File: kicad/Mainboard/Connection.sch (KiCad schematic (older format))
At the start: 12 parts, among them J13 DBG_CONN, J15 Micro_SD_Card

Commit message: Annotated parts, again.
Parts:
- gave numbers to parts that had none: 10
- renumbered J15 to J14, J13 to J15
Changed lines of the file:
@@
 EESchema Schematic File Version 4
-LIBS:Mainboard-cache
 EELAYER 30 0
 EELAYER END
@@
 $EndDescr
 $Comp
-L power:+5V #PWR0104
+L power:+5V #PWR0155
 U 1 1 5E07BDC5
 P 3000 1750
-F 0 "#PWR0104" H 3000 1600 50  0001 C CNN
+F 0 "#PWR0155" H 3000 1600 50  0001 C CNN
 F 1 "+5V" H 3015 1923 50  0000 C CNN
 F 2 "" H 3000 1750 50  0001 C CNN
@@
 	3000 1850 3100 1850
 $Comp
-L power:GND #PWR0106
+L power:GND #PWR0156
 U 1 1 5E07C3FA
 P 3000 2350
-F 0 "#PWR0106" H 3000 2100 50  0001 C CNN
+F 0 "#PWR0156" H 3000 2100 50  0001 C CNN
 F 1 "GND" H 3005 2177 50  0000 C CNN
 F 2 "" H 3000 2350 50  0001 C CNN
@@
 USART1_RX
 $Comp
-L Mainboard-rescue:Conn_01x03-conn J13
+L Mainboard-rescue:Conn_01x03-conn J15
 U 1 1 5E07CB74
 P 4800 2150
-F 0 "J13" H 4880 2192 50  0000 L CNN
+F 0 "J15" H 4880 2192 50  0000 L CNN
 F 1 "DBG_CONN" H 4880 2101 50  0000 L CNN
 F 2 "" H 4800 2150 50  0001 C CNN
@@
 USART2_RX
 $Comp
-L power:GND #PWR0107
+L power:GND #PWR0157
 U 1 1 5E07D3F6
 P 4500 2350
-F 0 "#PWR0107" H 4500 2100 50  0001 C CNN
+F 0 "#PWR0157" H 4500 2100 50  0001 C CNN
 F 1 "GND" H 4505 2177 50  0000 C CNN
 F 2 "" H 4500 2350 50  0001 C CNN
@@
 	4500 2050 4600 2050
 $Comp
-L Mainboard-rescue:Micro_SD_Card-conn J15
+L Mainboard-rescue:Micro_SD_Card-conn J14
 U 1 1 5E0856B5
 P 3950 3900
-F 0 "J15" H 3900 4617 50  0000 C CNN
+F 0 "J14" H 3900 4617 50  0000 C CNN
 F 1 "Micro_SD_Card" H 3900 4526 50  0000 C CNN
 F 2 "" H 5100 4200 50  0001 C CNN
@@
 	3050 4100 2950 4100
 $Comp
-L power:GND #PWR0114
+L power:GND #PWR0154
 U 1 1 5E08619F
 P 2950 4600
-F 0 "#PWR0114" H 2950 4350 50  0001 C CNN
+F 0 "#PWR0154" H 2950 4350 50  0001 C CNN
 F 1 "GND" H 2955 4427 50  0000 C CNN
 F 2 "" H 2950 4600 50  0001 C CNN
@@
 	2950 4100 2950 4600
 $Comp
-L power:GND #PWR0115
+L power:GND #PWR0158
 U 1 1 5E086C12
 P 4850 4600
-F 0 "#PWR0115" H 4850 4350 50  0001 C CNN
+F 0 "#PWR0158" H 4850 4350 50  0001 C CNN
 F 1 "GND" H 4855 4427 50  0000 C CNN
 F 2 "" H 4850 4600 50  0001 C CNN
@@
 	4850 4500 4850 4600
 $Comp
-L power:+3V3 #PWR0109
+L power:+3V3 #PWR0153
 U 1 1 5E087582
 P 2950 3500
-F 0 "#PWR0109" H 2950 3350 50  0001 C CNN
+F 0 "#PWR0153" H 2950 3350 50  0001 C CNN
 F 1 "+3V3" H 2965 3673 50  0000 C CNN
 F 2 "" H 2950 3500 50  0001 C CNN
@@
 ADDR 0x6B AG, 0x1E M
 $Comp
-L Sensor_Motion:LSM9DS1 U?
+L Sensor_Motion:LSM9DS1 U11
 U 1 1 5E067250
 P 8400 3850
-F 0 "U?" H 8400 3900 50  0000 C CNN
+F 0 "U11" H 8400 3900 50  0000 C CNN
 F 1 "LSM9DS1" H 8400 3800 50  0000 C CNN
 F 2 "Package_LGA:LGA-24L_3x3.5mm_P0.43mm" H 9900 4600 50  0001 C CNN
@@
 $EndComp
 $Comp
-L power:+3V3 #PWR?
+L power:+3V3 #PWR0166
 U 1 1 5E06CB2E
 P 8400 2850
-F 0 "#PWR?" H 8400 2700 50  0001 C CNN
+F 0 "#PWR0166" H 8400 2700 50  0001 C CNN
 F 1 "+3V3" H 8415 3023 50  0000 C CNN
 F 2 "" H 8400 2850 50  0001 C CNN
@@
 Connection ~ 8700 2950
 $Comp
-L power:GND #PWR?
+L power:GND #PWR0165
 U 1 1 5E06F5C7
 P 8300 4850
-F 0 "#PWR?" H 8300 4600 50  0001 C CNN
+F 0 "#PWR0165" H 8300 4600 50  0001 C CNN
 F 1 "GND" H 8305 4677 50  0000 C CNN
 F 2 "" H 8300 4850 50  0001 C CNN
@@
 $EndComp
 $Comp
-L power:GND #PWR?
+L power:GND #PWR0167
 U 1 1 5E06FFF0
 P 8500 4850
-F 0 "#PWR?" H 8500 4600 50  0001 C CNN
+F 0 "#PWR0167" H 8500 4600 50  0001 C CNN
 F 1 "GND" H 8505 4677 50  0000 C CNN
 F 2 "" H 8500 4850 50  0001 C CNN
@@
 $EndComp
 $Comp
-L power:GND #PWR?
+L power:GND #PWR0169
 U 1 1 5E070F61
 P 9200 4850
-F 0 "#PWR?" H 9200 4600 50  0001 C CNN
+F 0 "#PWR0169" H 9200 4600 50  0001 C CNN
 F 1 "GND" H 9205 4677 50  0000 C CNN
 F 2 "" H 9200 4850 50  0001 C CNN
@@
 	9200 4050 9200 4150
 $Comp
-L Device:R_Small R?
+L Device:R_Small R54
 U 1 1 5E07451A
 P 7500 3250
-F 0 "R?" H 7559 3296 50  0000 L CNN
+F 0 "R54" H 7559 3296 50  0000 L CNN
 F 1 "4k7" H 7559 3205 50  0000 L CNN
 F 2 "" H 7500 3250 50  0001 C CNN
@@
 $EndComp
 $Comp
-L Device:R_Small R?
+L Device:R_Small R53
 U 1 1 5E075066
 P 7250 3250
-F 0 "R?" H 7309 3296 50  0000 L CNN
+F 0 "R53" H 7309 3296 50  0000 L CNN
 F 1 "4k7" H 7309 3205 50  0000 L CNN
 F 2 "" H 7250 3250 50  0001 C CNN
@@
 Connection ~ 7500 3550
 $Comp
-L power:+3V3 #PWR?
+L power:+3V3 #PWR0163
 U 1 1 5E0788C1
 P 7500 3050
-F 0 "#PWR?" H 7500 2900 50  0001 C CNN
+F 0 "#PWR0163" H 7500 2900 50  0001 C CNN
 F 1 "+3V3" H 7515 3223 50  0000 C CNN
 F 2 "" H 7500 3050 50  0001 C CNN
@@
 $EndComp
 $Comp
-L power:+3V3 #PWR?
+L power:+3V3 #PWR0162
 U 1 1 5E078F90
 P 7250 3050
-F 0 "#PWR?" H 7250 2900 50  0001 C CNN
+F 0 "#PWR0162" H 7250 2900 50  0001 C CNN
 F 1 "+3V3" H 7265 3223 50  0000 C CNN
 F 2 "" H 7250 3050 50  0001 C CNN
@@
 	7500 3050 7500 3150
 $Comp
-L Device:C_Small C?
+L Device:C_Small C93
 U 1 1 5E07AC5C
 P 7500 4650
-F 0 "C?" H 7592 4696 50  0000 L CNN
+F 0 "C93" H 7592 4696 50  0000 L CNN
 F 1 "100n" H 7592 4605 50  0000 L CNN
 F 2 "" H 7500 4650 50  0001 C CNN
@@
 $EndComp
 $Comp
-L Device:C_Small C?
+L Device:C_Small C92
 U 1 1 5E07BBD5
 P 7150 4650
-F 0 "C?" H 7242 4696 50  0000 L CNN
+F 0 "C92" H 7242 4696 50  0000 L CNN
 F 1 "10n" H 7242 4605 50  0000 L CNN
 F 2 "" H 7150 4650 50  0001 C CNN
@@
 	7500 4450 7500 4550
 $Comp
-L power:GND #PWR?
+L power:GND #PWR0164
 U 1 1 5E07DD63
 P 7500 4850
-F 0 "#PWR?" H 7500 4600 50  0001 C CNN
+F 0 "#PWR0164" H 7500 4600 50  0001 C CNN
 F 1 "GND" H 7505 4677 50  0000 C CNN
 F 2 "" H 7500 4850 50  0001 C CNN
@@
 $EndComp
 $Comp
-L power:GND #PWR?
+L power:GND #PWR0161
 U 1 1 5E07E2EE
 P 7150 4850
-F 0 "#PWR?" H 7150 4600 50  0001 C CNN
+F 0 "#PWR0161" H 7150 4600 50  0001 C CNN
 F 1 "GND" H 7155 4677 50  0000 C CNN
 F 2 "" H 7150 4850 50  0001 C CNN
@@
 	9200 4350 9200 4850
 $Comp
-L Device:R_Small R?
+L Device:R_Small R52
 U 1 1 5E085D7F
 P 6950 3250
-F 0 "R?" H 7009 3296 50  0000 L CNN
+F 0 "R52" H 7009 3296 50  0000 L CNN
 F 1 "10k" H 7009 3205 50  0000 L CNN
 F 2 "" H 6950 3250 50  0001 C CNN
@@
 $EndComp
 $Comp
-L Device:R_Small R?
+L Device:R_Small R55
 U 1 1 5E086057
 P 9200 3250
-F 0 "R?" H 9259 3296 50  0000 L CNN
+F 0 "R55" H 9259 3296 50  0000 L CNN
 F 1 "10k" H 9259 3205 50  0000 L CNN
 F 2 "" H 9200 3250 50  0001 C CNN
@@
 	9200 3450 9200 3350
 $Comp
-L power:+3V3 #PWR?
+L power:+3V3 #PWR0160
 U 1 1 5E089278
 P 6950 3050
-F 0 "#PWR?" H 6950 2900 50  0001 C CNN
+F 0 "#PWR0160" H 6950 2900 50  0001 C CNN
 F 1 "+3V3" H 6965 3223 50  0000 C CNN
 F 2 "" H 6950 3050 50  0001 C CNN
@@
 	6950 3050 6950 3150
 $Comp
-L power:+3V3 #PWR?
+L power:+3V3 #PWR0168
 U 1 1 5E08A7A1
 P 9200 3050
-F 0 "#PWR?" H 9200 2900 50  0001 C CNN
+F 0 "#PWR0168" H 9200 2900 50  0001 C CNN
 F 1 "+3V3" H 9215 3223 50  0000 C CNN
 F 2 "" H 9200 3050 50  0001 C CNN
@@
 NoConn ~ 9100 3650
 $Comp
-L Device:R_Small R?
+L Device:R_Small R56
 U 1 1 5E0918A1
 P 9450 3250
-F 0 "R?" H 9509 3296 50  0000 L CNN
+F 0 "R56" H 9509 3296 50  0000 L CNN
 F 1 "10k" H 9509 3205 50  0000 L CNN
 F 2 "" H 9450 3250 50  0001 C CNN
@@
 	9450 3550 9450 3350
 $Comp
-L Device:R_Small R?
+L Device:R_Small R51
 U 1 1 5E092F27
 P 6700 3250
-F 0 "R?" H 6759 3296 50  0000 L CNN
+F 0 "R51" H 6759 3296 50  0000 L CNN
 F 1 "10k" H 6759 3205 50  0000 L CNN
 F 2 "" H 6700 3250 50  0001 C CNN
@@
 	6700 3850 6700 3350
 $Comp
-L power:+3V3 #PWR?
+L power:+3V3 #PWR0159
 U 1 1 5E09497A
 P 6700 3050
-F 0 "#PWR?" H 6700 2900 50  0001 C CNN
+F 0 "#PWR0159" H 6700 2900 50  0001 C CNN
 F 1 "+3V3" H 6715 3223 50  0000 C CNN
 F 2 "" H 6700 3050 50  0001 C CNN
@@
 	6700 3050 6700 3150
 $Comp
-L power:+3V3 #PWR?
+L power:+3V3 #PWR0170
 U 1 1 5E09620D
 P 9450 3050
-F 0 "#PWR?" H 9450 2900 50  0001 C CNN
+F 0 "#PWR0170" H 9450 2900 50  0001 C CNN
 F 1 "+3V3" H 9465 3223 50  0000 C CNN
 F 2 "" H 9450 3050 50  0001 C CNN
@@
 	6600 3550 7500 3550
 $Comp
-L Connector_Generic:Conn_01x05 J?
+L Connector_Generic:Conn_01x05 J13
 U 1 1 5E3E7A55
 P 3300 2050
-F 0 "J?" H 3380 2092 50  0000 L CNN
+F 0 "J13" H 3380 2092 50  0000 L CNN
 F 1 "GPS_CONN" H 3380 2001 50  0000 L CNN
 F 2 "" H 3300 2050 50  0001 C CNN

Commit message: Started assigning footprints
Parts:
- C92, C93: footprint (none) -> Capacitor_SMD:C_0603_1608Metric; symbol Device:C_Small -> Mainboard-rescue:C_Small-Device
- J13: symbol Connector_Generic:Conn_01x05 -> Mainboard-rescue:Conn_01x05-Connector_Generic
- R51, R52, R53, R54, R55, R56: symbol Device:R_Small -> Mainboard-rescue:R_Small-Device
- U11: symbol Sensor_Motion:LSM9DS1 -> Mainboard-rescue:LSM9DS1-Sensor_Motion
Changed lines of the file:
@@
 ADDR 0x6B AG, 0x1E M
 $Comp
-L Sensor_Motion:LSM9DS1 U11
+L Mainboard-rescue:LSM9DS1-Sensor_Motion U11
 U 1 1 5E067250
 P 8400 3850
@@
 	9200 4050 9200 4150
 $Comp
-L Device:R_Small R54
+L Mainboard-rescue:R_Small-Device R54
 U 1 1 5E07451A
 P 7500 3250
@@
 $EndComp
 $Comp
-L Device:R_Small R53
+L Mainboard-rescue:R_Small-Device R53
 U 1 1 5E075066
 P 7250 3250
@@
 	7500 3050 7500 3150
 $Comp
-L Device:C_Small C93
+L Mainboard-rescue:C_Small-Device C93
 U 1 1 5E07AC5C
 P 7500 4650
 F 0 "C93" H 7592 4696 50  0000 L CNN
 F 1 "100n" H 7592 4605 50  0000 L CNN
-F 2 "" H 7500 4650 50  0001 C CNN
+F 2 "Capacitor_SMD:C_0603_1608Metric" H 7500 4650 50  0001 C CNN
 F 3 "~" H 7500 4650 50  0001 C CNN
 	1    7500 4650
@@
 $EndComp
 $Comp
-L Device:C_Small C92
+L Mainboard-rescue:C_Small-Device C92
 U 1 1 5E07BBD5
 P 7150 4650
 F 0 "C92" H 7242 4696 50  0000 L CNN
 F 1 "10n" H 7242 4605 50  0000 L CNN
-F 2 "" H 7150 4650 50  0001 C CNN
+F 2 "Capacitor_SMD:C_0603_1608Metric" H 7150 4650 50  0001 C CNN
 F 3 "~" H 7150 4650 50  0001 C CNN
 	1    7150 4650
@@
 	9200 4350 9200 4850
 $Comp
-L Device:R_Small R52
+L Mainboard-rescue:R_Small-Device R52
 U 1 1 5E085D7F
 P 6950 3250
@@
 $EndComp
 $Comp
-L Device:R_Small R55
+L Mainboard-rescue:R_Small-Device R55
 U 1 1 5E086057
 P 9200 3250
@@
 NoConn ~ 9100 3650
 $Comp
-L Device:R_Small R56
+L Mainboard-rescue:R_Small-Device R56
 U 1 1 5E0918A1
 P 9450 3250
@@
 	9450 3550 9450 3350
 $Comp
-L Device:R_Small R51
+L Mainboard-rescue:R_Small-Device R51
 U 1 1 5E092F27
 P 6700 3250
@@
 	6600 3550 7500 3550
 $Comp
-L Connector_Generic:Conn_01x05 J13
+L Mainboard-rescue:Conn_01x05-Connector_Generic J13
 U 1 1 5E3E7A55
 P 3300 2050

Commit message: Add files via upload
assigned some more footprints
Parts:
- J15: footprint (none) -> Connector_PinHeader_2.54mm:PinHeader_1x03_P2.54mm_Vertical
- R51, R52, R53, R54, R55, R56: footprint (none) -> Resistor_SMD:R_0603_1608Metric
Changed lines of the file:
@@
 F 0 "J15" H 4880 2192 50  0000 L CNN
 F 1 "DBG_CONN" H 4880 2101 50  0000 L CNN
-F 2 "" H 4800 2150 50  0001 C CNN
+F 2 "Connector_PinHeader_2.54mm:PinHeader_1x03_P2.54mm_Vertical" H 4800 2150 50  0001 C CNN
 F 3 "~" H 4800 2150 50  0001 C CNN
 	1    4800 2150
@@
 F 0 "R54" H 7559 3296 50  0000 L CNN
 F 1 "4k7" H 7559 3205 50  0000 L CNN
-F 2 "" H 7500 3250 50  0001 C CNN
+F 2 "Resistor_SMD:R_0603_1608Metric" H 7500 3250 50  0001 C CNN
 F 3 "~" H 7500 3250 50  0001 C CNN
 	1    7500 3250
@@
 F 0 "R53" H 7309 3296 50  0000 L CNN
 F 1 "4k7" H 7309 3205 50  0000 L CNN
-F 2 "" H 7250 3250 50  0001 C CNN
+F 2 "Resistor_SMD:R_0603_1608Metric" H 7250 3250 50  0001 C CNN
 F 3 "~" H 7250 3250 50  0001 C CNN
 	1    7250 3250
@@
 F 0 "R52" H 7009 3296 50  0000 L CNN
 F 1 "10k" H 7009 3205 50  0000 L CNN
-F 2 "" H 6950 3250 50  0001 C CNN
+F 2 "Resistor_SMD:R_0603_1608Metric" H 6950 3250 50  0001 C CNN
 F 3 "~" H 6950 3250 50  0001 C CNN
 	1    6950 3250
@@
 F 0 "R55" H 9259 3296 50  0000 L CNN
 F 1 "10k" H 9259 3205 50  0000 L CNN
-F 2 "" H 9200 3250 50  0001 C CNN
+F 2 "Resistor_SMD:R_0603_1608Metric" H 9200 3250 50  0001 C CNN
 F 3 "~" H 9200 3250 50  0001 C CNN
 	1    9200 3250
@@
 F 0 "R56" H 9509 3296 50  0000 L CNN
 F 1 "10k" H 9509 3205 50  0000 L CNN
-F 2 "" H 9450 3250 50  0001 C CNN
+F 2 "Resistor_SMD:R_0603_1608Metric" H 9450 3250 50  0001 C CNN
 F 3 "~" H 9450 3250 50  0001 C CNN
 	1    9450 3250
@@
 F 0 "R51" H 6759 3296 50  0000 L CNN
 F 1 "10k" H 6759 3205 50  0000 L CNN
-F 2 "" H 6700 3250 50  0001 C CNN
+F 2 "Resistor_SMD:R_0603_1608Metric" H 6700 3250 50  0001 C CNN
 F 3 "~" H 6700 3250 50  0001 C CNN
 	1    6700 3250

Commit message: - Added footprint library - TR-9 - Imported a few footprints - Designed a MicroSD card slot footprint - Assignment footprints to corresponding elements on schematic
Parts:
- J14: footprint (none) -> TR-9:microSD
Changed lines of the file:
@@
 EESchema Schematic File Version 4
-LIBS:Mainboard-cache
 EELAYER 30 0
 EELAYER END
@@
 F 0 "J14" H 3900 4617 50  0000 C CNN
 F 1 "Micro_SD_Card" H 3900 4526 50  0000 C CNN
-F 2 "" H 5100 4200 50  0001 C CNN
+F 2 "TR-9:microSD" H 5100 4200 50  0001 C CNN
 F 3 "http://katalog.we-online.de/em/datasheet/693072010801.pdf" H 3950 3900 50  0001 C CNN
 	1    3950 3900

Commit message: - designed and added footprint for L8 RF inductor
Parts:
- J13: footprint (none) -> Connector_PinHeader_1.27mm:PinHeader_1x05_P1.27mm_Vertical
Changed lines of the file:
@@
 F 0 "J13" H 3380 2092 50  0000 L CNN
 F 1 "GPS_CONN" H 3380 2001 50  0000 L CNN
-F 2 "" H 3300 2050 50  0001 C CNN
+F 2 "Connector_PinHeader_1.27mm:PinHeader_1x05_P1.27mm_Vertical" H 3300 2050 50  0001 C CNN
 F 3 "~" H 3300 2050 50  0001 C CNN
 	1    3300 2050

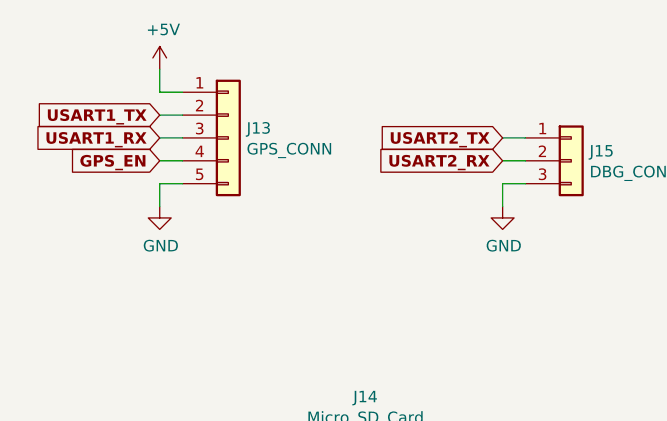
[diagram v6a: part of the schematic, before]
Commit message: Added thermal vias to BGA6589 footprint Corrected USART to UART
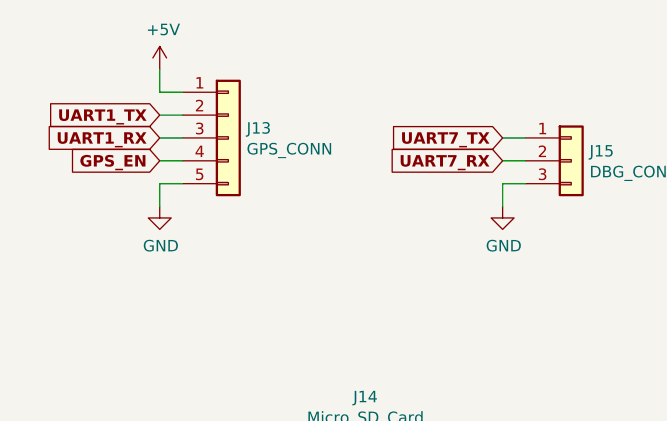
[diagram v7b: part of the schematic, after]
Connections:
- net USART1_RX renamed UART1_RX
- net USART1_TX renamed UART1_TX
- net USART2_RX renamed UART7_RX
- net USART2_TX renamed UART7_TX
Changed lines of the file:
@@
 	3100 2050 3000 2050
 Text GLabel 3000 1950 0    50   Input ~ 10
-USART1_TX
+UART1_TX
 Text GLabel 3000 2050 0    50   Input ~ 10
-USART1_RX
+UART1_RX
 $Comp
 L Mainboard-rescue:Conn_01x03-conn J15
@@
 $EndComp
 Text GLabel 4500 2050 0    50   Input ~ 10
-USART2_TX
+UART7_TX
 Text GLabel 4500 2150 0    50   Input ~ 10
-USART2_RX
+UART7_RX
 $Comp
 L power:GND #PWR0157

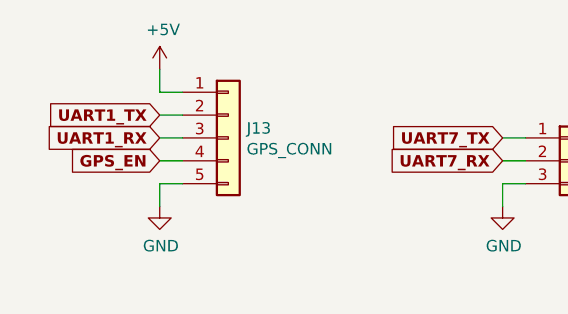
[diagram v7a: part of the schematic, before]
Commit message: started working on PCB - power supply completed plotted new PDF schematic
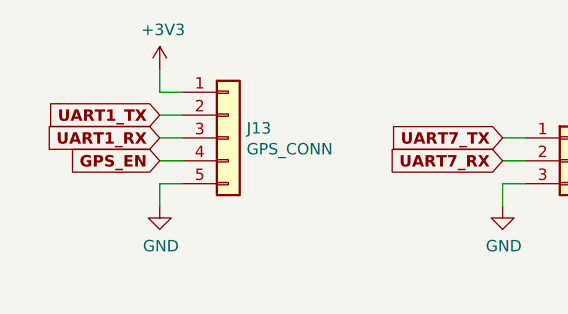
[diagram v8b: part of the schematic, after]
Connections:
- net +5V is gone; now on net +3V3: J13.1 (Pin_1)
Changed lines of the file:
@@
 Comment4 "TR-9 Open Source Digital Radio"
 $EndDescr
-$Comp
-L power:+5V #PWR0155
-U 1 1 5E07BDC5
-P 3000 1750
-F 0 "#PWR0155" H 3000 1600 50  0001 C CNN
-F 1 "+5V" H 3015 1923 50  0000 C CNN
-F 2 "" H 3000 1750 50  0001 C CNN
-F 3 "" H 3000 1750 50  0001 C CNN
-	1    3000 1750
-	1    0    0    -1
-$EndComp
 Wire Wire Line
 	3000 1750 3000 1850
@@
 Text GLabel 3000 2150 0    50   Input ~ 10
 GPS_EN
+$Comp
+L power:+3V3 #PWR?
+U 1 1 5E4F7B10
+P 3000 1750
+AR Path="/5DEDCA32/5E4F7B10" Ref="#PWR?"  Part="1"
+AR Path="/5E07B88F/5E4F7B10" Ref="#PWR?"  Part="1"
+F 0 "#PWR?" H 3000 1600 50  0001 C CNN
+F 1 "+3V3" H 3015 1923 50  0000 C CNN
+F 2 "" H 3000 1750 50  0001 C CNN
+F 3 "" H 3000 1750 50  0001 C CNN
+	1    3000 1750
+	1    0    0    -1
+$EndComp
 $EndSCHEMATC
